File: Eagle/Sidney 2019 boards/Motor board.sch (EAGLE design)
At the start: 39 parts, among them IC1 LM2596S, IC2 LM2940CS-5.0_NOPB

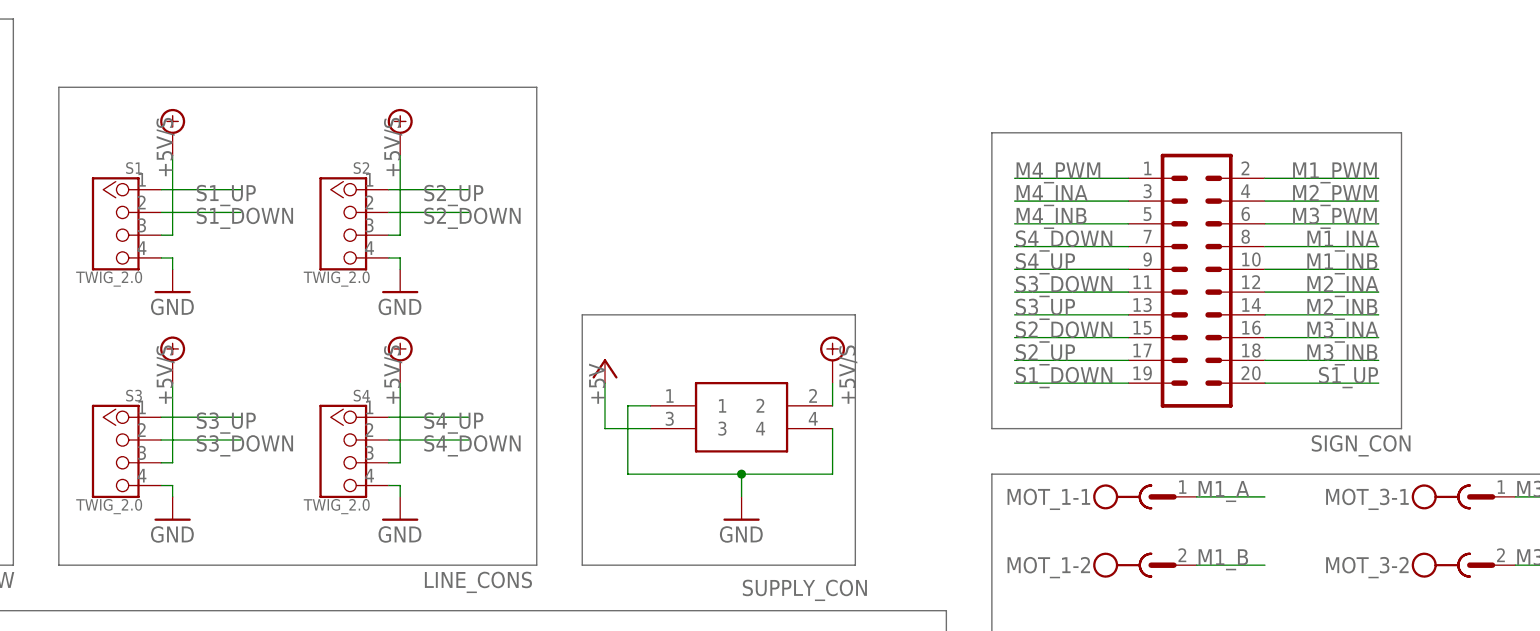
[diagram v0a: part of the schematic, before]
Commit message: Finished components lists for both boards and fixed line sensors' connectors pinout
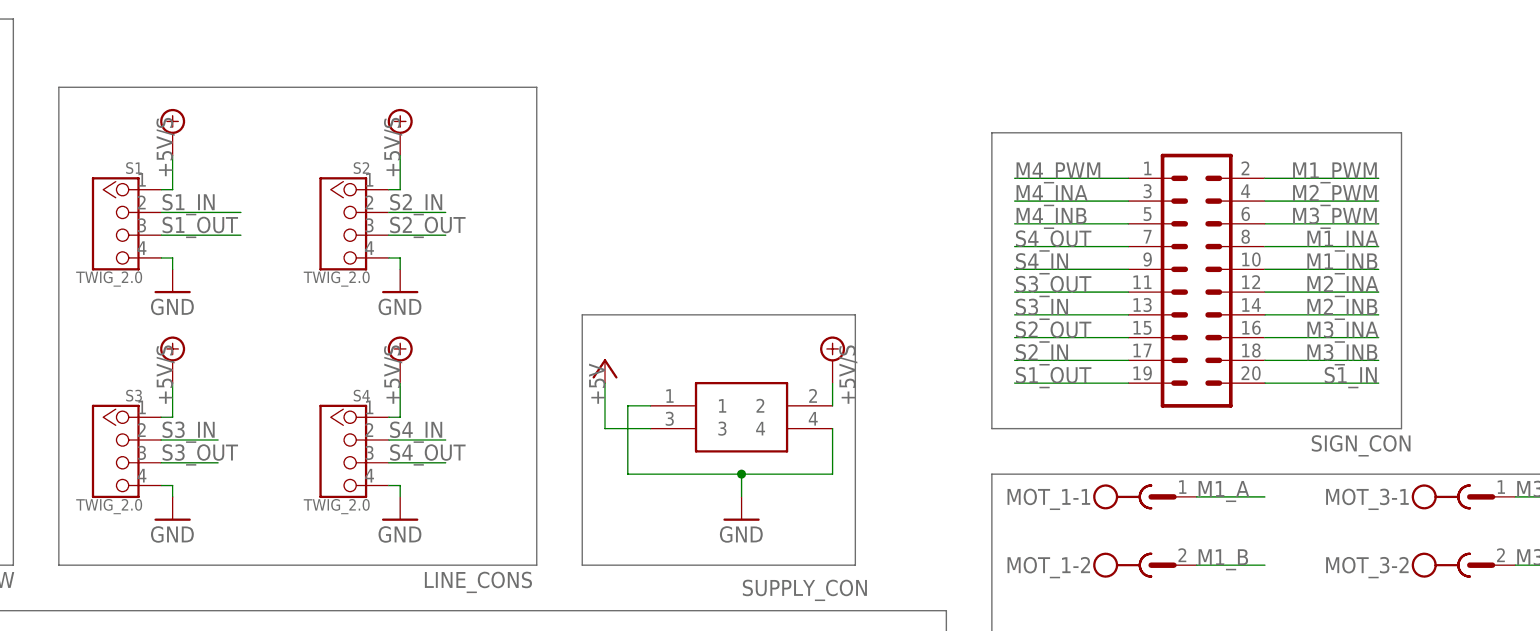
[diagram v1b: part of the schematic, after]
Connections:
- removed net S1_DOWN: S1.2, SIGN_CON.19
- removed net S1_UP: S1.1, SIGN_CON.20
- removed net S2_DOWN: S2.2, SIGN_CON.15
- removed net S2_UP: S2.1, SIGN_CON.17
- removed net S3_DOWN: S3.2, SIGN_CON.11
- removed net S3_UP: S3.1, SIGN_CON.13
- removed net S4_DOWN: S4.2, SIGN_CON.7
- removed net S4_UP: S4.1, SIGN_CON.9
- new net S1_IN: S1.2, SIGN_CON.20
- new net S1_OUT: S1.3, SIGN_CON.19
- new net S2_IN: S2.2, SIGN_CON.17
- new net S2_OUT: S2.3, SIGN_CON.15
- new net S3_IN: S3.2, SIGN_CON.13
- new net S3_OUT: S3.3, SIGN_CON.11
- new net S4_IN: S4.2, SIGN_CON.9
- new net S4_OUT: S4.3, SIGN_CON.7
- net +5V/S: now also S1.1, S2.1, S3.1, S4.1; no longer S1.3, S2.3, S3.3, S4.3

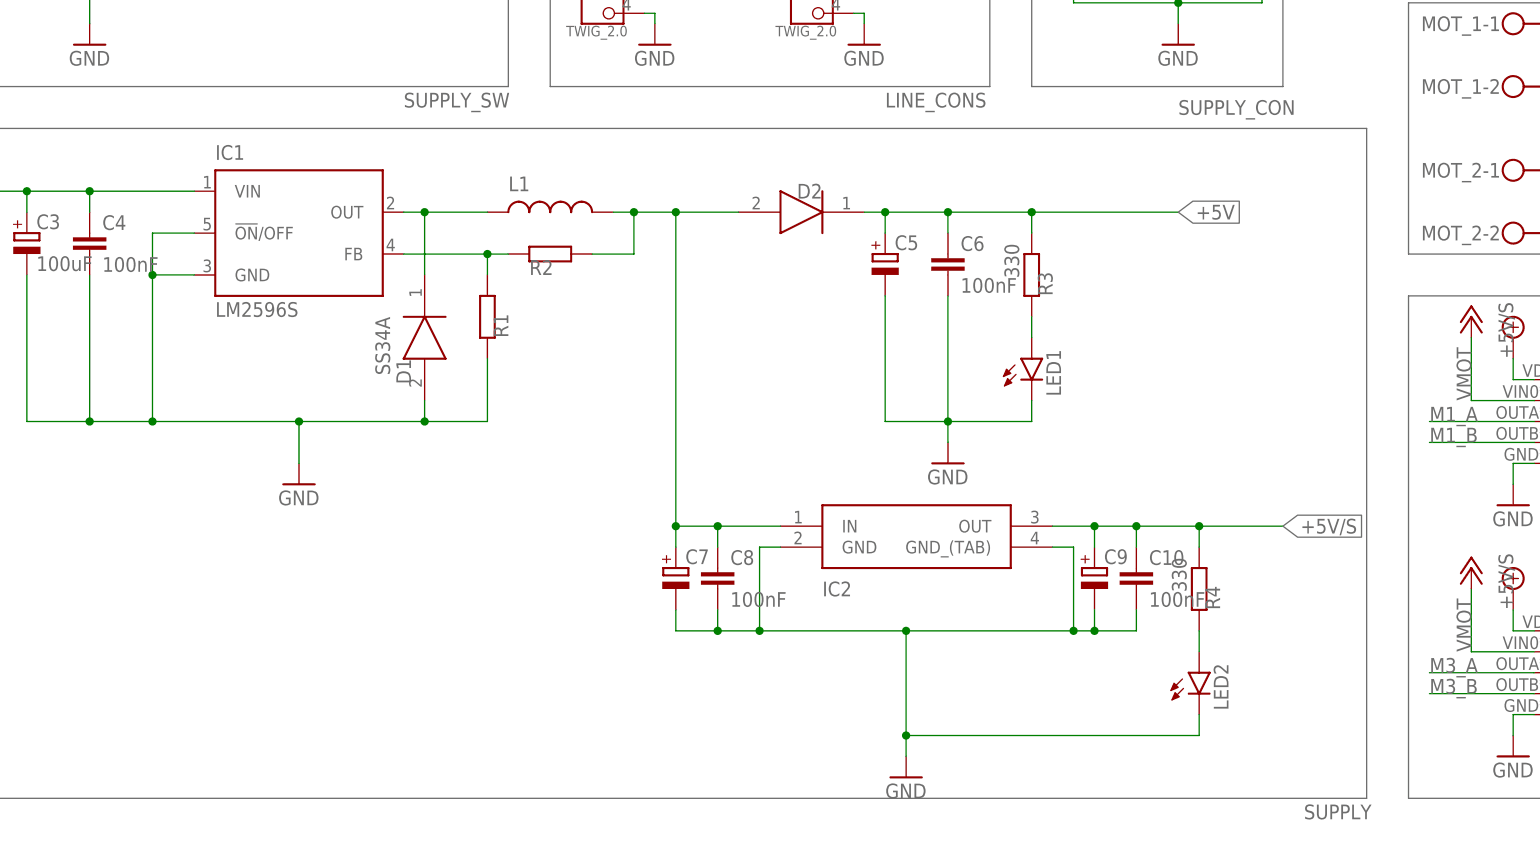
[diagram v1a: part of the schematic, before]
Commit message: Finished motor board, deleted useless files, added parts in components lists for both boards and other stuff
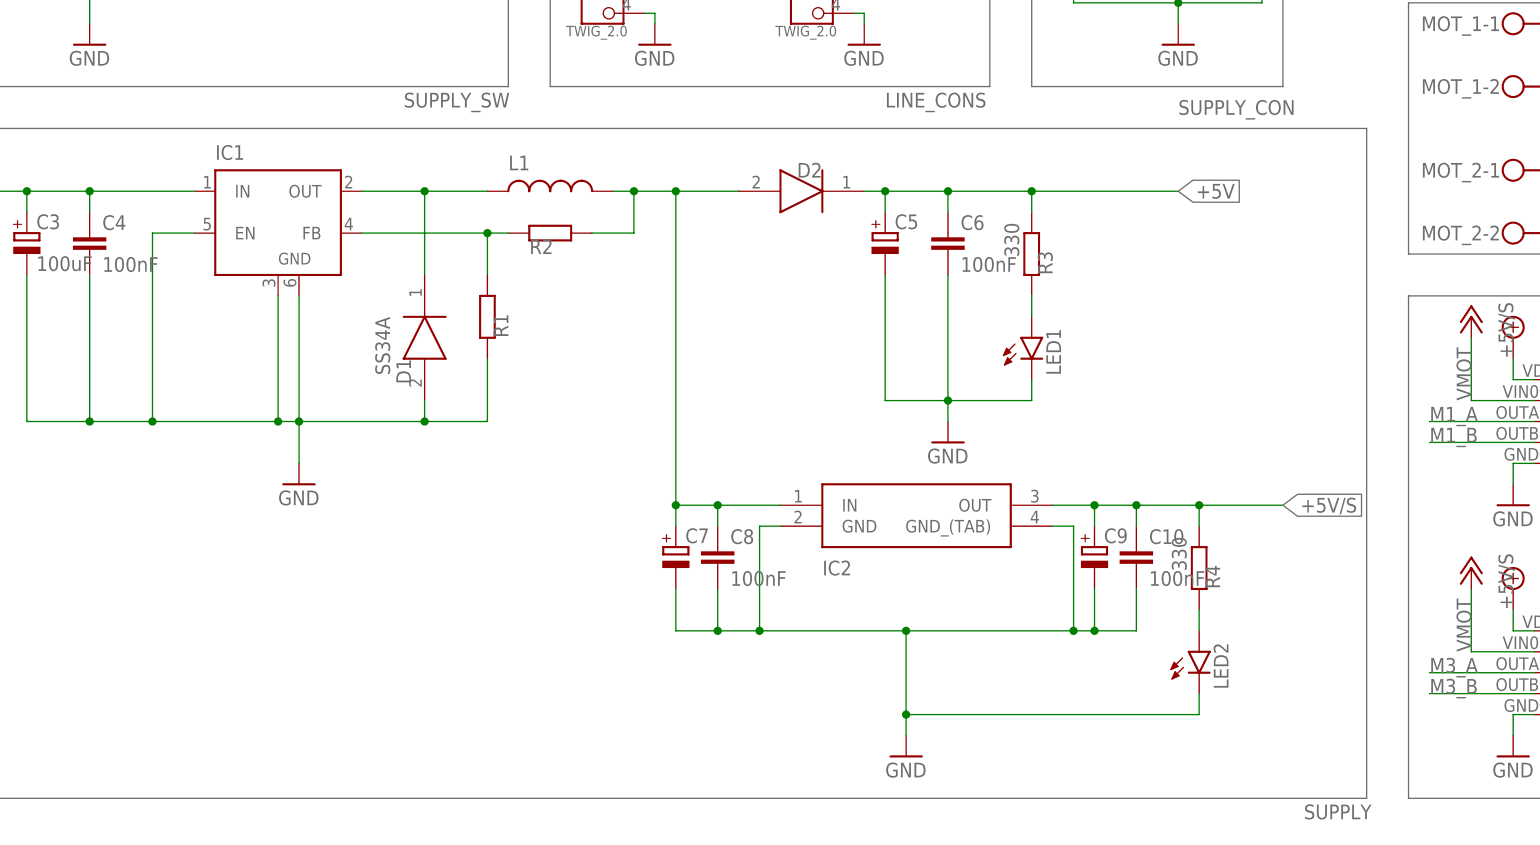
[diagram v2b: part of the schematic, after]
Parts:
- IC1: value LM2596S -> (none); device national-semiconductor:LM2596S -> linear:LM2596S
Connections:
- net GND: now also IC1.EN, IC1.GND@1; no longer IC1.!ON!/OFF
- net VCC: now also IC1.IN; no longer IC1.VIN
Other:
- moved on the sheet: C10, C5, C6, C7, C8, C9, D2, IC2, L1, LED1, LED2, R2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

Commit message: Added grove connectors for auxiliary supply
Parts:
- added SUPPLY2_CON: TWIG_2.0, CONNECTER:TWIG_2.0
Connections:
- net +5V: now also SUPPLY2_CON.1
- net +5V/S: now also SUPPLY2_CON.3
- net GND: now also SUPPLY2_CON.2, SUPPLY2_CON.4
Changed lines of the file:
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@@
 <setting verticaltext="up"/>
 </settings>
-<grid distance="0.1" unitdist="inch" unit="inch" style="lines" multiple="1" display="no" altdistance="0.01" altunitdist="inch" altunit="inch"/>
+<grid distance="0.1" unitdist="inch" unit="inch" style="lines" multiple="1" display="yes" altdistance="0.01" altunitdist="inch" altunit="inch"/>
 <layers>
 <layer number="1" name="Top" color="4" fill="1" visible="no" active="no"/>
@@
 <part name="BAT_-" library="wirepad" library_urn="urn:adsk.eagle:library:412" deviceset="3,81/1,4" device="" package3d_urn="urn:adsk.eagle:package:30835/1"/>
 <part name="IC1" library="linear" library_urn="urn:adsk.eagle:library:262" deviceset="LM2596S" device="" package3d_urn="urn:adsk.eagle:package:16438/2"/>
+<part name="SUPPLY2_CON" library="CONNECTER" deviceset="TWIG_2.0" device=""/>
+<part name="P+6" library="supply1" library_urn="urn:adsk.eagle:library:371" deviceset="+5V" device=""/>
+<part name="SUPPLY10" library="supply2" library_urn="urn:adsk.eagle:library:372" deviceset="+5V/1" device=""/>
+<part name="GND12" library="supply1" library_urn="urn:adsk.eagle:library:371" deviceset="GND" device=""/>
 </parts>
 <sheets>
@@
 <text x="279.4" y="0" size="1.778" layer="95">MOTOR_DRIVERS</text>
 <wire x1="170.18" y1="88.9" x2="170.18" y2="116.84" width="0.1524" layer="95"/>
+<wire x1="139.7" y1="147.32" x2="162.56" y2="147.32" width="0.1524" layer="95"/>
+<wire x1="162.56" y1="147.32" x2="162.56" y2="121.92" width="0.1524" layer="95"/>
+<wire x1="162.56" y1="121.92" x2="139.7" y2="121.92" width="0.1524" layer="95"/>
+<wire x1="139.7" y1="121.92" x2="139.7" y2="147.32" width="0.1524" layer="95"/>
 </plain>
 <instances>
@@
 <attribute name="NAME" x="40.64" y="80.01" size="1.778" layer="95"/>
 <attribute name="VALUE" x="50.8" y="80.01" size="1.778" layer="96"/>
+</instance>
+<instance part="SUPPLY2_CON" gate="G$1" x="147.32" y="134.62" smashed="yes" rot="MR0">
+<attribute name="NAME" x="162.56" y="119.38" size="1.27" layer="95" rot="MR0"/>
+<attribute name="VALUE" x="149.098" y="128.016" size="1.27" layer="96" rot="MR0"/>
+</instance>
+<instance part="P+6" gate="1" x="154.94" y="144.78" smashed="yes">
+<attribute name="VALUE" x="154.94" y="138.43" size="1.778" layer="96" rot="R90"/>
+</instance>
+<instance part="SUPPLY10" gate="G$1" x="158.75" y="142.24" smashed="yes"/>
+<instance part="GND12" gate="1" x="153.67" y="127" smashed="yes">
+<attribute name="VALUE" x="151.13" y="124.46" size="1.778" layer="96"/>
 </instance>
 </instances>
@@
 <wire x1="256.54" y1="12.7" x2="256.54" y2="10.16" width="0.1524" layer="91"/>
 </segment>
+<segment>
+<pinref part="SUPPLY2_CON" gate="G$1" pin="2"/>
+<pinref part="GND12" gate="1" pin="GND"/>
+<wire x1="151.13" y1="135.89" x2="153.67" y2="135.89" width="0.1524" layer="91"/>
+<wire x1="153.67" y1="135.89" x2="153.67" y2="130.81" width="0.1524" layer="91"/>
+<pinref part="SUPPLY2_CON" gate="G$1" pin="4"/>
+<wire x1="153.67" y1="130.81" x2="153.67" y2="129.54" width="0.1524" layer="91"/>
+<wire x1="151.13" y1="130.81" x2="153.67" y2="130.81" width="0.1524" layer="91"/>
+<junction x="153.67" y="130.81"/>
+</segment>
 </net>
 <net name="+5V" class="0">
@@
 <pinref part="SUPPLY_CON" gate="G$1" pin="3"/>
 <wire x1="142.24" y1="104.14" x2="147.32" y2="104.14" width="0.1524" layer="91"/>
+</segment>
+<segment>
+<pinref part="P+6" gate="1" pin="+5V"/>
+<wire x1="154.94" y1="142.24" x2="154.94" y2="138.43" width="0.1524" layer="91"/>
+<pinref part="SUPPLY2_CON" gate="G$1" pin="1"/>
+<wire x1="154.94" y1="138.43" x2="151.13" y2="138.43" width="0.1524" layer="91"/>
 </segment>
 </net>
@@
 <label x="256.54" y="25.4" size="1.778" layer="95" rot="R90"/>
 </segment>
+<segment>
+<pinref part="SUPPLY10" gate="G$1" pin="+5V/1"/>
+<pinref part="SUPPLY2_CON" gate="G$1" pin="3"/>
+<wire x1="158.75" y1="139.7" x2="158.75" y2="133.35" width="0.1524" layer="91"/>
+<wire x1="158.75" y1="133.35" x2="151.13" y2="133.35" width="0.1524" layer="91"/>
+<label x="158.75" y="134.874" size="1.778" layer="95" rot="R90"/>
+</segment>
 </net>
